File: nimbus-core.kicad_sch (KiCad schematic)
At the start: 69 parts, among them J1 QTE-020-03-L-D-A, J2 QSE-020-01-L-D-A, J3 532614006, J4 USB4105-GF-A-120, J5 532614006, J6 532614006, U1 ${MANUFACTURER PART NUMBER}, U10 ${COLOR}, U4 SN65HVD233-Q1, U8 SN65HVD1782-Q1, U9 USBLC6-2P6, Y1 25MHz

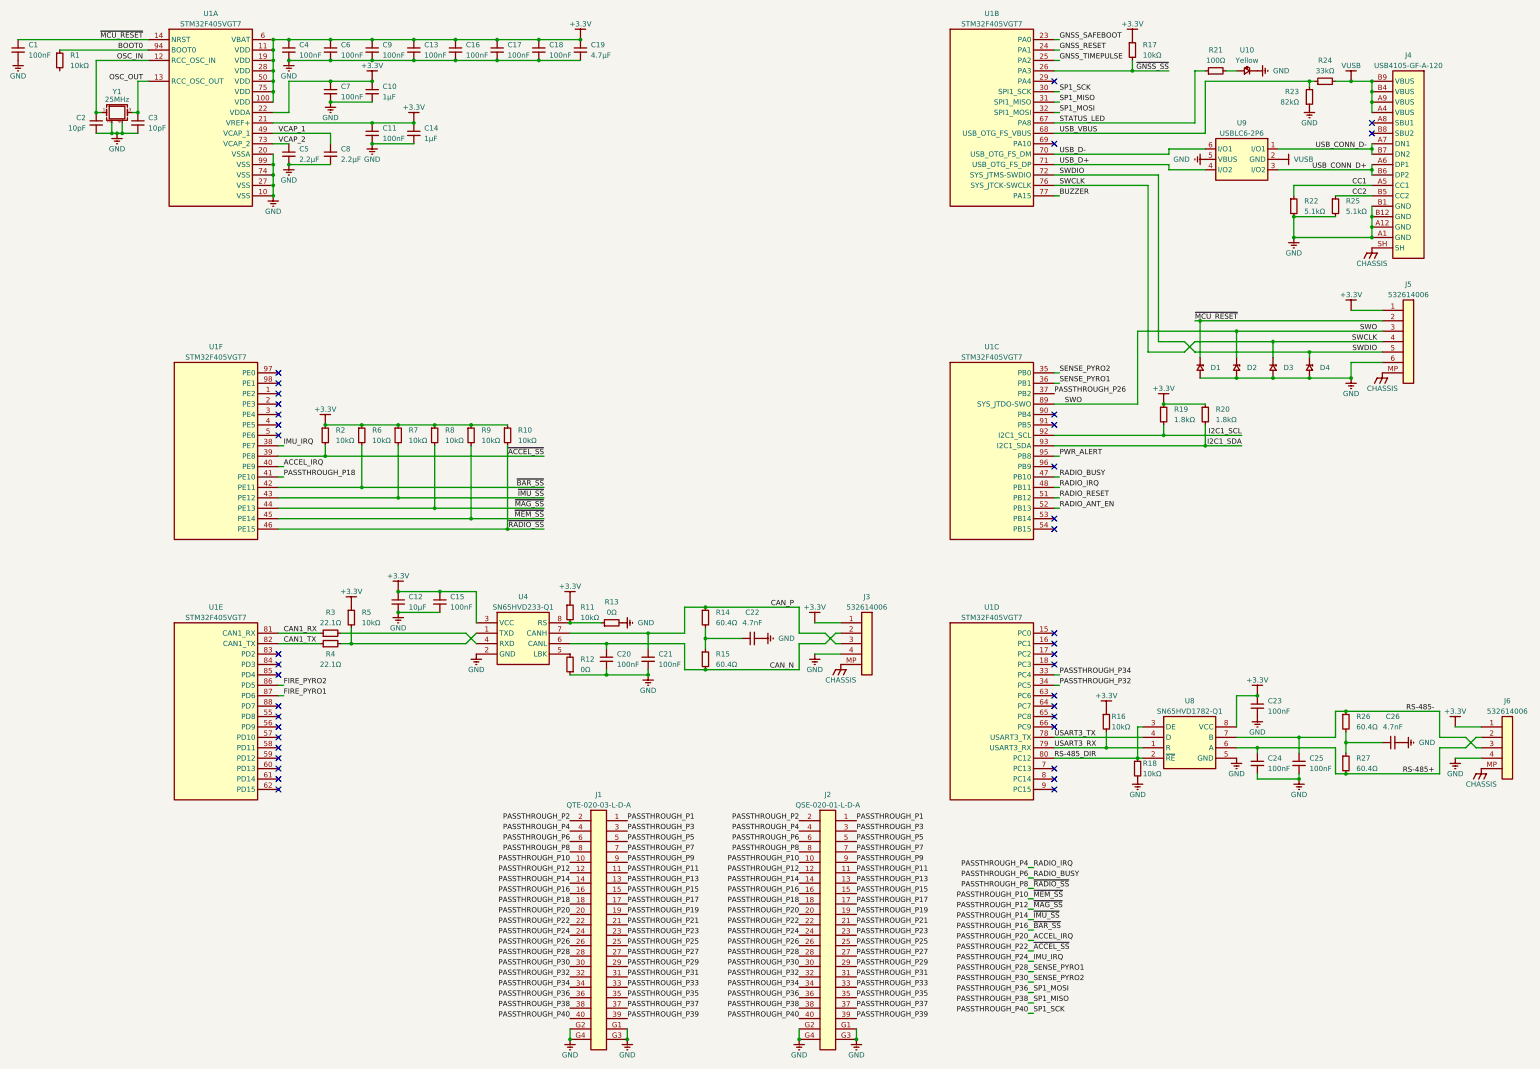
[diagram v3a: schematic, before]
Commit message: Shift passthrough pinout by 1 to insert another pin
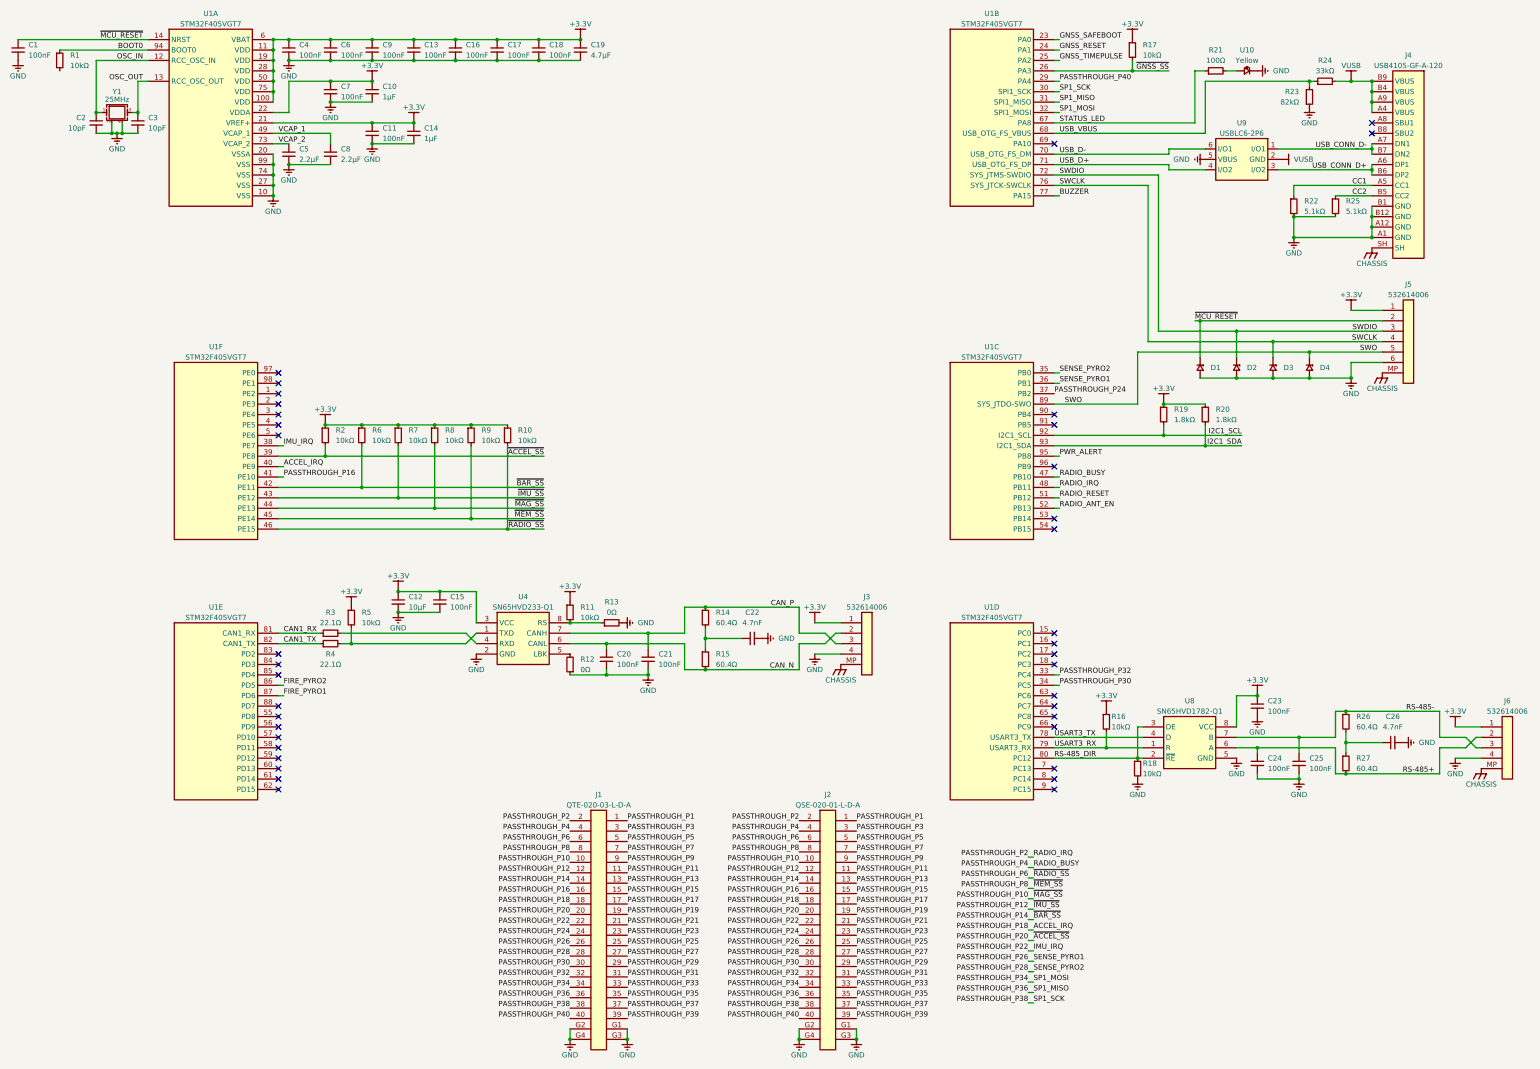
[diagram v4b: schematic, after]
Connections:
- net ACCEL_IRQ: now also J1.18, J2.18; no longer J1.20, J2.20
- net IMU_IRQ: now also J1.22, J2.22; no longer J1.24, J2.24
- net PASSTHROUGH_P10: now also R8.2, U1.44 (PE13); no longer R9.2, U1.45 (PE14)
- net PASSTHROUGH_P12: now also R7.2, U1.43 (PE12); no longer R8.2, U1.44 (PE13)
- net PASSTHROUGH_P14: now also R6.2, U1.42 (PE11); no longer R7.2, U1.43 (PE12)
- net PASSTHROUGH_P16: now also U1.41 (PE10); no longer R6.2, U1.42 (PE11)
- net PASSTHROUGH_P2: now also U1.48 (PB11)
- net PASSTHROUGH_P26: now also U1.36 (PB1); no longer U1.37 (PB2)
- net PASSTHROUGH_P28: now also U1.35 (PB0); no longer U1.36 (PB1)
- net PASSTHROUGH_P30: now also U1.34 (PC5); no longer U1.35 (PB0)
- net PASSTHROUGH_P32: now also U1.33 (PC4); no longer U1.34 (PC5)
- net PASSTHROUGH_P34: now also U1.32 (PA7); no longer U1.33 (PC4)
- net PASSTHROUGH_P36: now also U1.31 (PA6); no longer U1.32 (PA7)
- net PASSTHROUGH_P38: now also U1.30 (PA5); no longer U1.31 (PA6)
- net PASSTHROUGH_P4: now also U1.47 (PB10); no longer U1.48 (PB11)
- net PASSTHROUGH_P40: now also U1.29 (PA4); no longer U1.30 (PA5)
- net PASSTHROUGH_P6: now also R10.2, U1.46 (PE15); no longer U1.47 (PB10)
- net PASSTHROUGH_P8: now also R9.2, U1.45 (PE14); no longer R10.2, U1.46 (PE15)
- net SWDIO: now also D2.1, J5.3; no longer D4.1, J5.5
- net SWO: now also D4.1, J5.5; no longer D2.1, J5.3
- removed net PASSTHROUGH_P18: J1.18, J2.18, U1.41 (PE10)
- net PASSTHROUGH_P22 renamed PASSTHROUGH_P20
- net PASSTHROUGH_P20: now also J1.20, J2.20; no longer J1.22, J2.22
- new net PASSTHROUGH_P24: J1.24, J2.24, U1.37 (PB2)
- no-connect marks 39 -> 38

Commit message: Rename all passthrough pins to their corresponding MCU pin name, fix typo on SPI pins
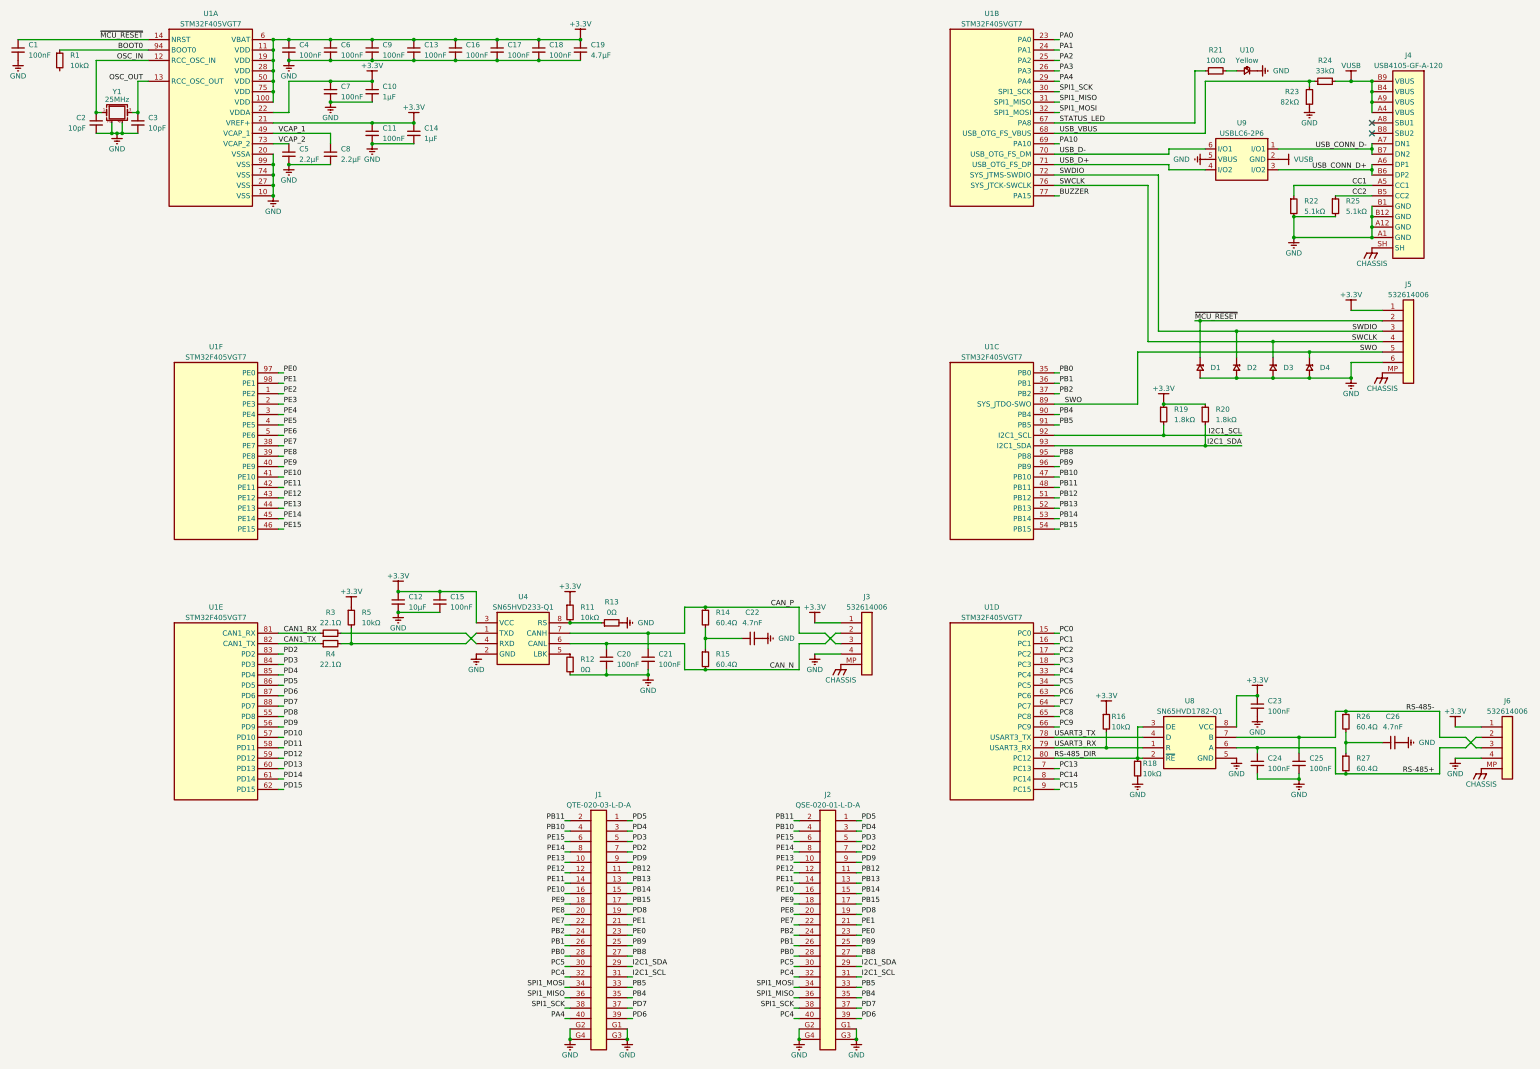
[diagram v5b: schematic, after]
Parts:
- removed R10, R17, R2, R6, R7, R8, R9: 10kΩ, passive:R_0603_Density_Nominal, symbol passive:CRCW060310K0FKEAHP
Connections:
- net PASSTHROUGH_P1 is gone; now on net PD5: J1.1, J2.1
- net PASSTHROUGH_P15 is gone; now on net PB14: J1.15, J2.15
- net PASSTHROUGH_P17 is gone; now on net PB15: J1.17, J2.17
- net PASSTHROUGH_P19 is gone; now on net PD8: J1.19, J2.19
- net PASSTHROUGH_P21 is gone; now on net PE1: J1.21, J2.21
- net PASSTHROUGH_P23 is gone; now on net PE0: J1.23, J2.23
- net PASSTHROUGH_P25 is gone; now on net PB9: J1.25, J2.25
- net PASSTHROUGH_P29 is gone; now on net I2C1_SDA: J1.29, J2.29
- net PASSTHROUGH_P3 is gone; now on net PD4: J1.3, J2.3
- net PASSTHROUGH_P31 is gone; now on net I2C1_SCL: J1.31, J2.31
- net PASSTHROUGH_P33 is gone; now on net PB5: J1.33, J2.33
- net PASSTHROUGH_P35 is gone; now on net PB4: J1.35, J2.35
- net PASSTHROUGH_P37 is gone; now on net PD7: J1.37, J2.37
- net PASSTHROUGH_P39 is gone; now on net PD6: J1.39, J2.39
- net PASSTHROUGH_P5 is gone; now on net PD3: J1.5, J2.5
- net PASSTHROUGH_P7 is gone; now on net PD2: J1.7, J2.7
- net PASSTHROUGH_P9 is gone; now on net PD9: J1.9, J2.9
- net PWR_ALERT is gone; now on net PB8: U1.95 (PB8)
- net RADIO_ANT_EN is gone; now on net PB13: U1.52 (PB13)
- net RADIO_RESET is gone; now on net PB12: U1.51 (PB12)
- net PA10: now reaches U1.69 (PA10)
- net PD8: now reaches U1.55 (PD8)
- net PD9: now reaches U1.56 (PD9)
- net PD10: now reaches U1.57 (PD10)
- net PD11: now reaches U1.58 (PD11)
- net PD12: now reaches U1.59 (PD12)
- net PD13: now reaches U1.60 (PD13)
- net PD14: now reaches U1.61 (PD14)
- net PD15: now reaches U1.62 (PD15)
- net PD2: now reaches U1.83 (PD2)
- net PD3: now reaches U1.84 (PD3)
- net PD4: now reaches U1.85 (PD4)
- net PD7: now reaches U1.88 (PD7)
- net PE2: now reaches U1.1 (PE2)
- net PE3: now reaches U1.2 (PE3)
- net PE4: now reaches U1.3 (PE4)
- net PE5: now reaches U1.4 (PE5)
- net PE6: now reaches U1.5 (PE6)
- net PE0: now reaches U1.97 (PE0)
- net PE1: now reaches U1.98 (PE1)
- net PB14: now reaches U1.53 (PB14)
- net PB15: now reaches U1.54 (PB15)
- net PB4: now reaches U1.90 (PB4)
- net PB5: now reaches U1.91 (PB5)
- net PB9: now reaches U1.96 (PB9)
- net PC0: now reaches U1.15 (PC0)
- net PC1: now reaches U1.16 (PC1)
- net PC2: now reaches U1.17 (PC2)
- net PC3: now reaches U1.18 (PC3)
- net PC6: now reaches U1.63 (PC6)
- net PC7: now reaches U1.64 (PC7)
- net PC8: now reaches U1.65 (PC8)
- net PC9: now reaches U1.66 (PC9)
- net PC13: now reaches U1.7 (PC13)
- net PC14: now reaches U1.8 (PC14)
- net PC15: now reaches U1.9 (PC15)
- net ACCEL_IRQ renamed PE9
- net FIRE_PYRO1 renamed PD6
- net FIRE_PYRO2 renamed PD5
- net GNSS_RESET renamed PA1
- net GNSS_SAFEBOOT renamed PA0
- net GNSS_TIMEPULSE renamed PA2
- net IMU_IRQ renamed PE7
- net PASSTHROUGH_P10 renamed PE13
- net PASSTHROUGH_P11 renamed PB12
- net PASSTHROUGH_P12 renamed PE12
- net PASSTHROUGH_P13 renamed PB13
- net PASSTHROUGH_P14 renamed PE11
- net PASSTHROUGH_P16 renamed PE10
- net PASSTHROUGH_P2 renamed PB11
- net PASSTHROUGH_P20 renamed PE8
- net PASSTHROUGH_P24 renamed PB2
- net PASSTHROUGH_P26 renamed PB1
- net PASSTHROUGH_P27 renamed PB8
- net PASSTHROUGH_P28 renamed PB0
- net PASSTHROUGH_P30 renamed PC5
- net PASSTHROUGH_P32 renamed PC4
- net PC4: now also J2.40
- net PASSTHROUGH_P34 renamed SPI1_MOSI
- net PASSTHROUGH_P36 renamed SPI1_MISO
- net PASSTHROUGH_P38 renamed SPI1_SCK
- net PASSTHROUGH_P4 renamed PB10
- net PASSTHROUGH_P40 renamed PA4
- net PA4: no longer J2.40
- net PASSTHROUGH_P6 renamed PE15
- net PASSTHROUGH_P8 renamed PE14
- net ~{GNSS_SS} renamed PA3
- no-connect marks 38 -> 2

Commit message: Updated kicad-library
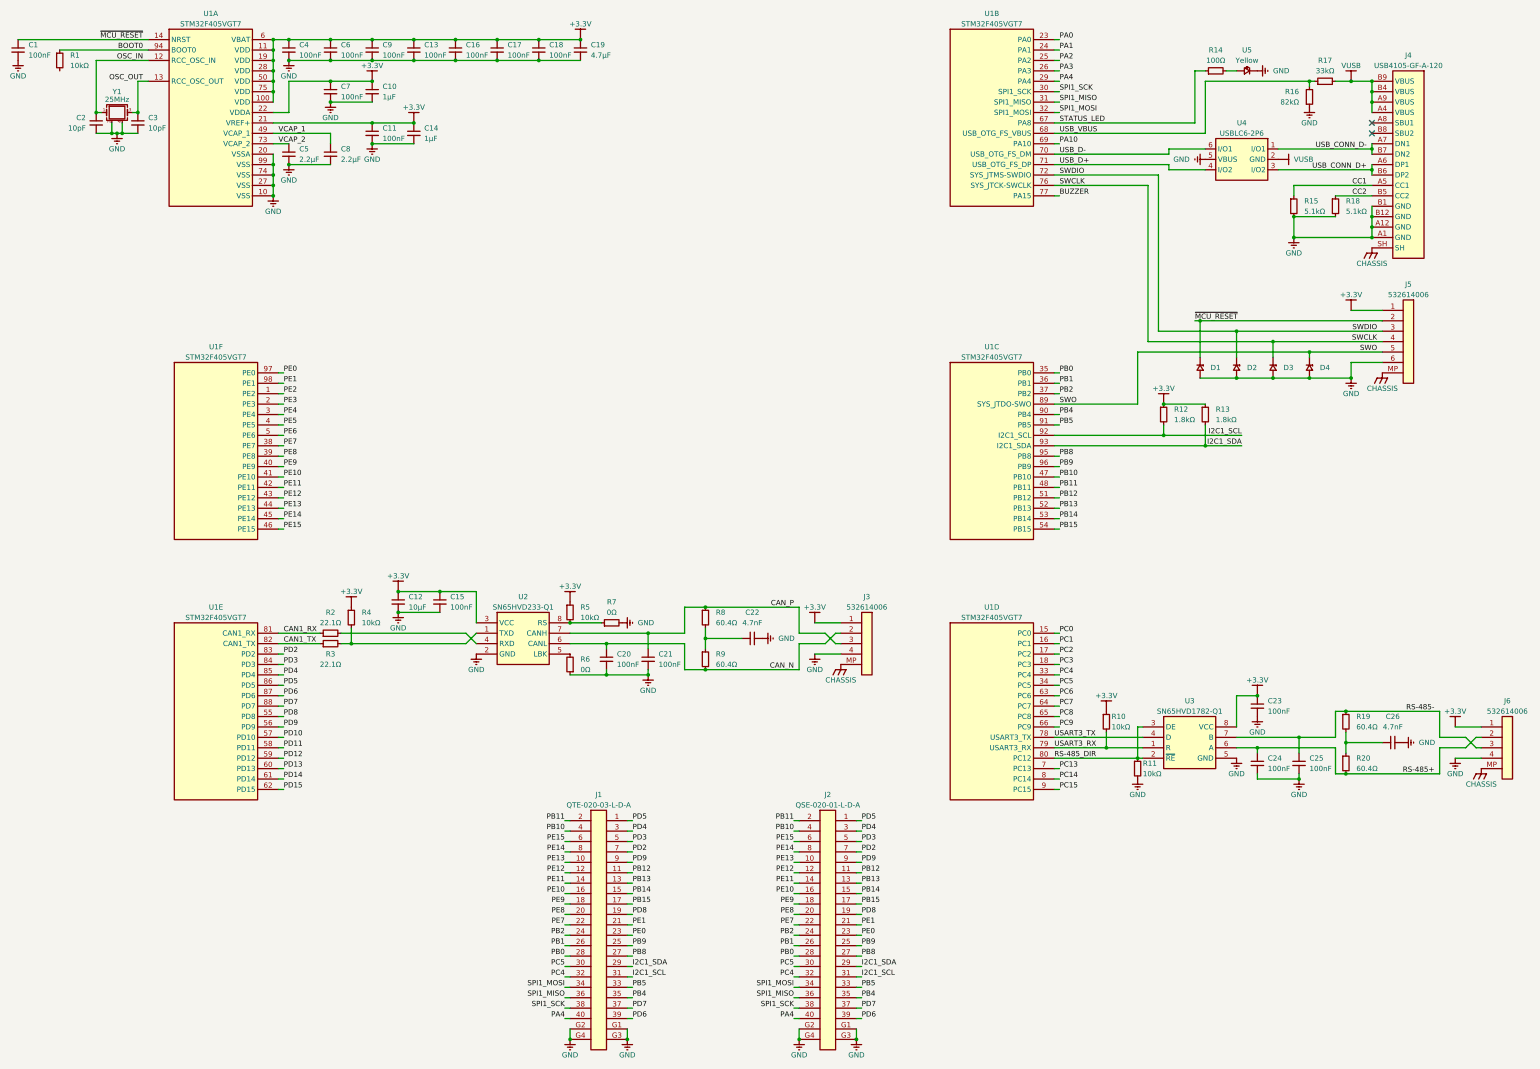
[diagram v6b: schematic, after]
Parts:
- renumbered R16 to R10, R18 to R11, R19 to R12, R20 to R13, R21 to R14, R22 to R15, R23 to R16, R24 to R17, R25 to R18, R26 to R19, R3 to R2, R27 to R20, R4 to R3, R5 to R4, R11 to R5, R12 to R6, R13 to R7, R14 to R8, R15 to R9, U4 to U2, U8 to U3, U9 to U4, U10 to U5
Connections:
- net PA4: now also J2.40
- net PC4: no longer J2.40
